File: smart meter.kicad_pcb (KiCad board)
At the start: 2 copper layers, 93 x 190.6 mm, 57 parts, among them J1 Energy_Meter_Conn, J2 Control_Terminal, J4 PV, J5 AC_Input, J6 DC_out, J7 Loads1, J8 Loads2, Q1 BTA41-600, Q2 BTA41-600, Q3 BTA41-600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

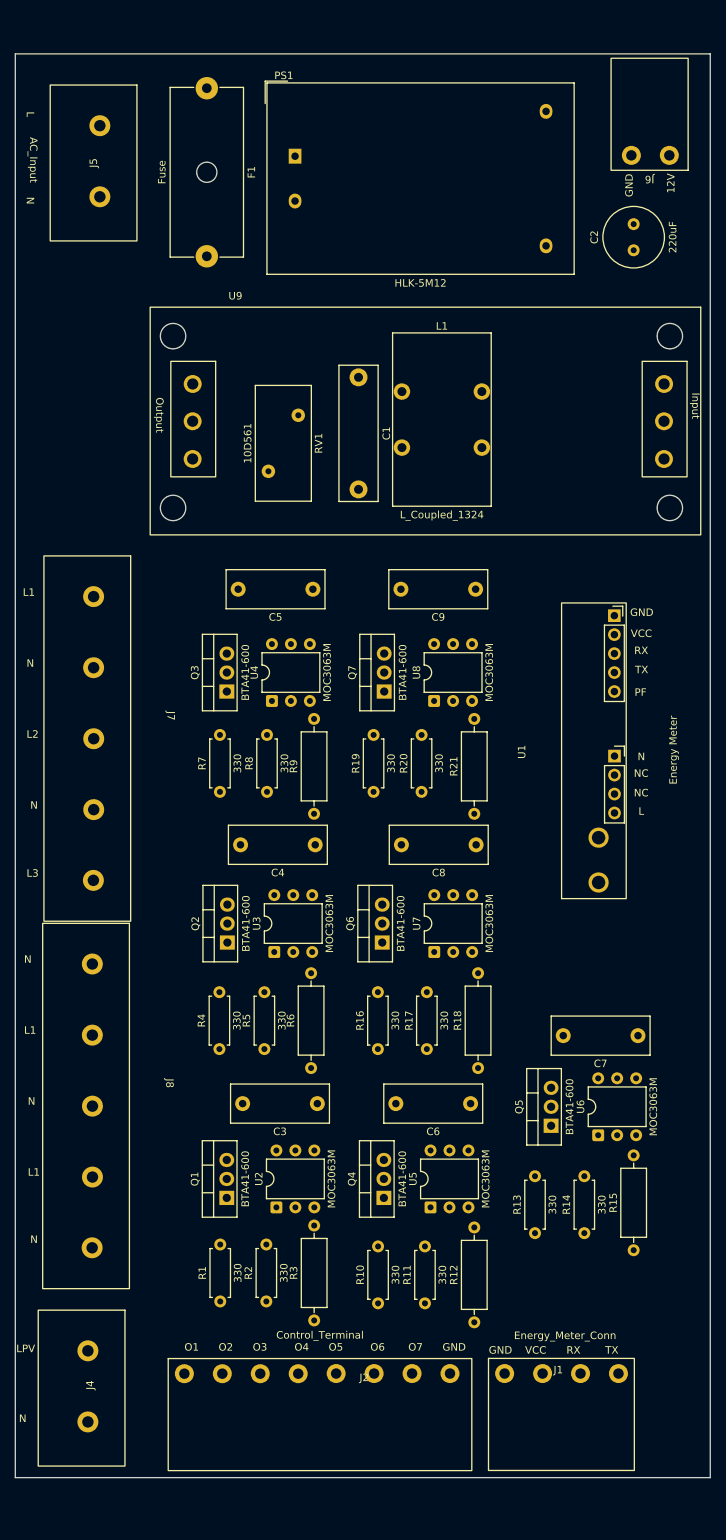
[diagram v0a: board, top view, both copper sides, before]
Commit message: Routing Power ctr
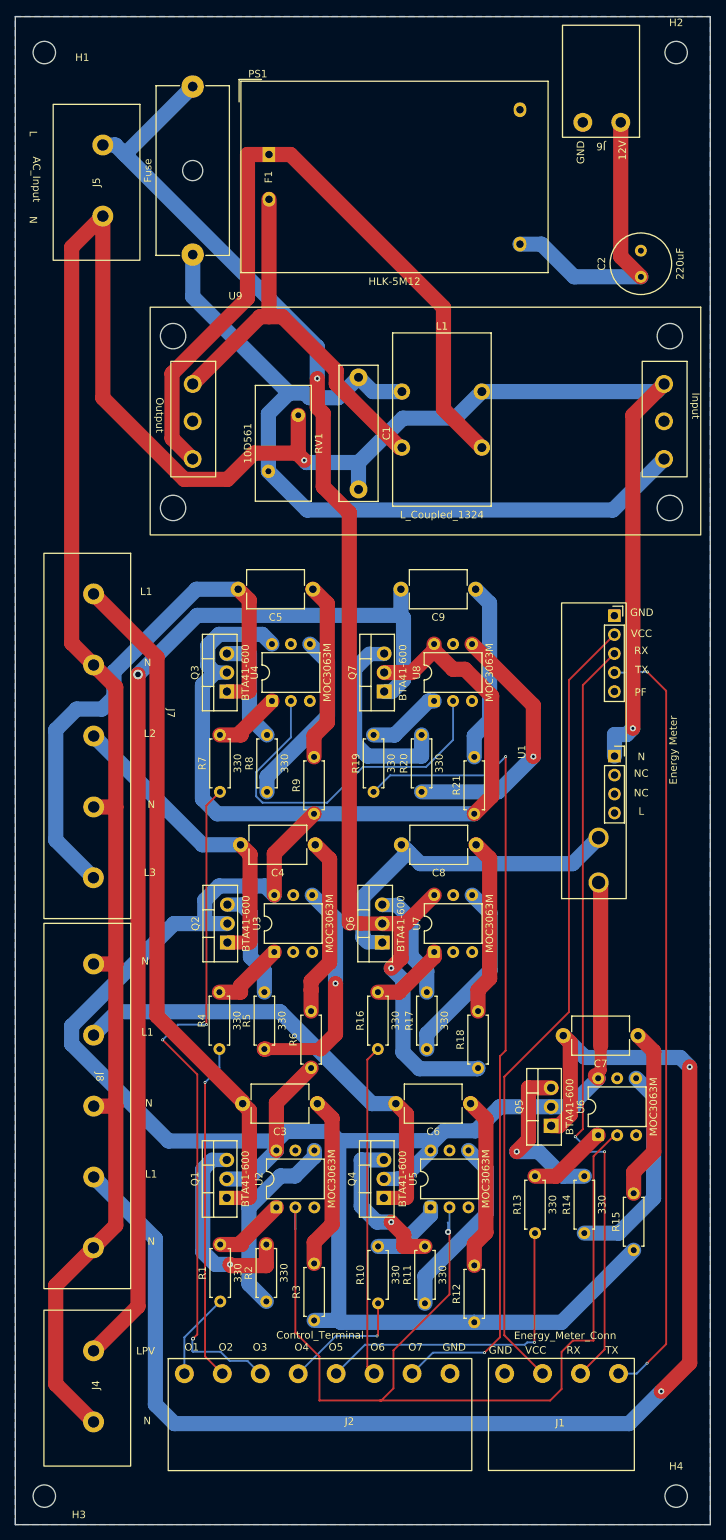
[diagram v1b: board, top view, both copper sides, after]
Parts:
- added H1: MountingHole, MountingHole:MountingHole_3mm, F.Cu at (152.2, 55.3)
- added H2: MountingHole, MountingHole:MountingHole_3mm, F.Cu at (236.8, 55.3)
- added H3: MountingHole, MountingHole:MountingHole_3mm, F.Cu at (152.2, 248.6)
- added H4: MountingHole, MountingHole:MountingHole_3mm, F.Cu at (236.8, 248.6)
- C3, C4, C5, C6, C7, C8, C9: footprint Capacitor_THT:C_Rect_L13.0mm_W5.0mm_P10.00mm_FKS3_FKP3_MKS4 -> Capacitor_THT:C_Disc_D7.5mm_W5.0mm_P10.00mm
- R12, R15, R18, R21, R3, R6, R9: footprint Resistor_THT:R_Axial_DIN0309_L9.0mm_D3.2mm_P12.70mm_Horizontal -> Resistor_THT:R_Axial_DIN0207_L6.3mm_D2.5mm_P7.62mm_Horizontal
- moved J6 7.86 mm to (226.7, 71.3)
- moved C2 3.68 mm to (232.1, 85.3)
- moved PS1 3.50 mm to (182.3, 69.0)
- moved J5 2.62 mm to (169.9, 72.2)
- moved F1 1.90 mm to (172.1, 59.9)
- moved J4 0.76 mm to (168.7, 233.6)
- moved J7 0.36 mm to (168.7, 143.8)
- moved J8 0.17 mm to (168.7, 193.3)
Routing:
- net /Meter_out: track 0.00 -> 371.7 mm
- net /N: track 0.00 -> 352.5 mm, vias 0 -> 2
- net /GND: track 0.00 -> 183.4 mm, vias 0 -> 1
- net /L5: track 0.00 -> 182.3 mm, vias 0 -> 2
- net /L: track 0.00 -> 174.1 mm, vias 0 -> 2
- net /Lpv: track 0.00 -> 147.0 mm, vias 0 -> 1
- net /O7: track 0.00 -> 111.5 mm, vias 0 -> 2
- net Net-(C1-Pad1): track 0.00 -> 110.7 mm
- net /VCC: track 0.00 -> 107.1 mm
- net /TX: track 0.00 -> 103.5 mm, vias 0 -> 2
- net /RX: track 0.00 -> 102.6 mm, vias 0 -> 2
- net Net-(PS1-AC/L): track 0.00 -> 101.7 mm
- net /O3: track 0.00 -> 92.8 mm, vias 0 -> 3
- net /L1: track 0.00 -> 92.5 mm
- net /L3: track 0.00 -> 73.4 mm
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- added copper zone on B.Cu, net /GND
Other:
- board size 93 x 190.6 mm -> 93 x 201.9 mm

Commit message: last update
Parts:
- C3, C4, C5, C6, C7, C8, C9: footprint Capacitor_THT:C_Disc_D7.5mm_W5.0mm_P10.00mm -> Capacitor_THT:C_Rect_L13.0mm_W5.0mm_P10.00mm_FKS3_FKP3_MKS4
- R12, R15, R18, R21, R3, R6, R9: footprint Resistor_THT:R_Axial_DIN0207_L6.3mm_D2.5mm_P7.62mm_Horizontal -> Resistor_THT:R_Axial_DIN0309_L9.0mm_D3.2mm_P12.70mm_Horizontal
- moved J6 8.03 mm to (226.4, 79.3)
- moved H3 7.30 mm to (155.9, 242.2)
- moved H4 6.38 mm to (237.5, 242.2)
- moved J4 6.17 mm to (168.3, 227.5)
- moved J7 5.00 mm to (168.7, 138.8)
- moved J8 4.31 mm to (168.6, 189.0)
- moved H2 3.73 mm to (237.2, 59.0)
- moved H1 3.71 mm to (152.4, 59.0)
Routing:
- net /Meter_out: track 371.7 -> 385.5 mm
- net Net-(R17-Pad1): track 25.1 -> 33.9 mm
- net /L1: track 92.5 -> 101.0 mm
- net /12V: track 39.8 -> 31.9 mm
- net /N: track 352.5 -> 359.2 mm
- net Net-(R8-Pad1): track 24.1 -> 30.3 mm
- net /Lpv: track 147.0 -> 141.0 mm
- net Net-(C6-Pad1): track 23.2 -> 18.1 mm
- net Net-(R11-Pad1): track 24.8 -> 29.9 mm
- net Net-(C4-Pad1): track 24.1 -> 19.6 mm
- net /L5: track 182.3 -> 186.6 mm
- net /O7: track 111.5 -> 115.4 mm
- net Net-(C7-Pad1): track 23.1 -> 19.3 mm
- net /L2: track 42.3 -> 46.0 mm
- net Net-(C3-Pad1): track 23.2 -> 20.4 mm
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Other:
- board size 93 x 201.9 mm -> 93 x 191.5 mm
- board text added: "L4"
- board text added: "L5"
